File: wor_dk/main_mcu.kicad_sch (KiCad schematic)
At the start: 36 parts, among them J201 Prog_DUT, SW201 SW_Push, U201 nRF52840, U202 TMUX1112PWR, U203 TMUX1112PWR, Y201 32.768kHz, Y202 32MHz

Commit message: wor_dk: add footprints & part info for all capacitors
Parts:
- C201, C202, C203, C206, C209, C217: MPN (none) -> GRM033R61E104KE14D
- C204, C218, C219: MPN (none) -> CL10A105KB8NNNC
- C205: MPN (none) -> CL10A475KO8NNNC
- C207: footprint Resistor_SMD:R_0603_1608Metric -> Capacitor_SMD:C_0603_1608Metric; MPN (none) -> CL10A105KB8NNNC
- C208: footprint Resistor_SMD:R_0201_0603Metric -> Capacitor_SMD:C_0201_0603Metric; MPN (none) -> GRT033R60J473KE01D
- C211: MPN (none) -> GRM0335C1H101JA01D
- C212: MPN (none) -> GRM033R71E821KA01D
- C213, C214: MPN (none) -> GCM1555C1H220FA16D
- C215, C216: MPN (none) -> GJM1555C1H130FB01D
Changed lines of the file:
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@@
 			)
 		)
-		(property "Datasheet" "~"
+		(property "Datasheet" "https://wmsc.lcsc.com/wmsc/upload/file/pdf/v2/lcsc/1811081532_Murata-Electronics-GRM033R61E104KE14D_C76939.pdf"
 			(at 31.75 167.64 0)
 			(effects
@@
 			)
 		)
+		(property "MPN" "GRM033R61E104KE14D"
+			(at 31.75 167.64 0)
+			(effects
+				(font
+					(size 1.27 1.27)
+				)
+				(hide yes)
+			)
+		)
 		(pin "1"
 		)
@@
 			)
 		)
-		(property "Datasheet" "~"
+		(property "Datasheet" "https://wmsc.lcsc.com/wmsc/upload/file/pdf/v2/lcsc/2304140030_Samsung-Electro-Mechanics-CL10A105KB8NNNC_C15849.pdf"
 			(at 238.76 95.25 0)
 			(effects
@@
 			)
 		)
+		(property "MPN" "CL10A105KB8NNNC"
+			(at 238.76 95.25 0)
+			(effects
+				(font
+					(size 1.27 1.27)
+				)
+				(hide yes)
+			)
+		)
 		(pin "1"
 		)
@@
 			)
 		)
-		(property "Datasheet" "~"
+		(property "Datasheet" "https://wmsc.lcsc.com/wmsc/upload/file/pdf/v2/lcsc/1811081532_Murata-Electronics-GRM033R61E104KE14D_C76939.pdf"
 			(at 162.56 24.13 0)
 			(effects
@@
 			)
 		)
+		(property "MPN" "GRM033R61E104KE14D"
+			(at 162.56 24.13 0)
+			(effects
+				(font
+					(size 1.27 1.27)
+				)
+				(hide yes)
+			)
+		)
 		(pin "1"
 		)
@@
 			)
 		)
-		(property "Datasheet" "~"
+		(property "Datasheet" "https://wmsc.lcsc.com/wmsc/upload/file/pdf/v2/lcsc/1811081545_Murata-Electronics-GRM033R71E821KA01D_C185597.pdf"
 			(at 49.53 44.45 0)
 			(effects
@@
 			)
 		)
+		(property "MPN" "GRM033R71E821KA01D"
+			(at 49.53 44.45 0)
+			(effects
+				(font
+					(size 1.27 1.27)
+				)
+				(hide yes)
+			)
+		)
 		(pin "1"
 		)
@@
 			)
 		)
-		(property "Datasheet" "~"
+		(property "Datasheet" "https://wmsc.lcsc.com/wmsc/upload/file/pdf/v2/lcsc/1811081532_Murata-Electronics-GRM033R61E104KE14D_C76939.pdf"
 			(at 113.03 24.13 0)
 			(effects
@@
 			)
 		)
+		(property "MPN" "GRM033R61E104KE14D"
+			(at 113.03 24.13 0)
+			(effects
+				(font
+					(size 1.27 1.27)
+				)
+				(hide yes)
+			)
+		)
 		(pin "1"
 		)
@@
 			)
 		)
+		(property "MPN" "GCM1555C1H220FA16D"
+			(at 156.21 60.96 0)
+			(effects
+				(font
+					(size 1.27 1.27)
+				)
+				(hide yes)
+			)
+		)
 		(pin "1"
 		)
@@
 			)
 		)
-		(property "Datasheet" "~"
+		(property "Datasheet" "https://wmsc.lcsc.com/wmsc/upload/file/pdf/v2/lcsc/1811081532_Murata-Electronics-GRM033R61E104KE14D_C76939.pdf"
 			(at 15.24 44.45 0)
 			(effects
@@
 			)
 		)
+		(property "MPN" "GRM033R61E104KE14D"
+			(at 15.24 44.45 0)
+			(effects
+				(font
+					(size 1.27 1.27)
+				)
+				(hide yes)
+			)
+		)
 		(pin "1"
 		)
@@
 			)
 		)
+		(property "MPN" "GJM1555C1H130FB01D"
+			(at 27.94 123.19 0)
+			(effects
+				(font
+					(size 1.27 1.27)
+				)
+				(hide yes)
+			)
+		)
 		(pin "1"
 		)
@@
 			)
 		)
+		(property "MPN" "GCM1555C1H220FA16D"
+			(at 156.21 50.8 0)
+			(effects
+				(font
+					(size 1.27 1.27)
+				)
+				(hide yes)
+			)
+		)
 		(pin "1"
 		)
@@
 			)
 		)
-		(property "Datasheet" "~"
+		(property "Datasheet" "https://wmsc.lcsc.com/wmsc/upload/file/pdf/v2/lcsc/2304140030_Samsung-Electro-Mechanics-CL10A105KB8NNNC_C15849.pdf"
 			(at 138.43 24.13 0)
 			(effects
@@
 			)
 		)
+		(property "MPN" "CL10A105KB8NNNC"
+			(at 138.43 24.13 0)
+			(effects
+				(font
+					(size 1.27 1.27)
+				)
+				(hide yes)
+			)
+		)
 		(pin "1"
 		)
@@
 			)
 		)
-		(property "Datasheet" "~"
+		(property "Datasheet" "https://wmsc.lcsc.com/wmsc/upload/file/pdf/v2/lcsc/1811081532_Murata-Electronics-GRM033R61E104KE14D_C76939.pdf"
 			(at 101.6 24.13 0)
 			(effects
@@
 			)
 		)
+		(property "MPN" "GRM033R61E104KE14D"
+			(at 101.6 24.13 0)
+			(effects
+				(font
+					(size 1.27 1.27)
+				)
+				(hide yes)
+			)
+		)
 		(pin "1"
 		)
@@
 			)
 		)
-		(property "Datasheet" "~"
+		(property "Datasheet" "https://wmsc.lcsc.com/wmsc/upload/file/pdf/v2/lcsc/1811081532_Murata-Electronics-GRM033R61E104KE14D_C76939.pdf"
 			(at 124.46 24.13 0)
 			(effects
@@
 			)
 		)
+		(property "MPN" "GRM033R61E104KE14D"
+			(at 124.46 24.13 0)
+			(effects
+				(font
+					(size 1.27 1.27)
+				)
+				(hide yes)
+			)
+		)
 		(pin "1"
 		)
@@
 			)
 		)
+		(property "MPN" "GJM1555C1H130FB01D"
+			(at 27.94 113.03 0)
+			(effects
+				(font
+					(size 1.27 1.27)
+				)
+				(hide yes)
+			)
+		)
 		(pin "1"
 		)
@@
 			)
 		)
-		(property "Footprint" "Resistor_SMD:R_0201_0603Metric"
+		(property "Footprint" "Capacitor_SMD:C_0201_0603Metric"
 			(at 216.8652 40.64 0)
 			(effects
@@
 			)
 		)
-		(property "Datasheet" "~"
+		(property "Datasheet" "https://wmsc.lcsc.com/wmsc/upload/file/pdf/v2/lcsc/1811141821_Murata-Electronics-GRT033R60J473KE01D_C126621.pdf"
 			(at 215.9 36.83 0)
 			(effects
@@
 			)
 		)
+		(property "MPN" "GRT033R60J473KE01D"
+			(at 215.9 36.83 0)
+			(effects
+				(font
+					(size 1.27 1.27)
+				)
+				(hide yes)
+			)
+		)
 		(pin "1"
 		)
@@
 			)
 		)
-		(property "Datasheet" "~"
+		(property "Datasheet" "https://wmsc.lcsc.com/wmsc/upload/file/pdf/v2/lcsc/2304140030_Samsung-Electro-Mechanics-CL10A105KB8NNNC_C15849.pdf"
 			(at 226.06 151.13 0)
 			(effects
@@
 			)
 		)
+		(property "MPN" "CL10A105KB8NNNC"
+			(at 226.06 151.13 0)
+			(effects
+				(font
+					(size 1.27 1.27)
+				)
+				(hide yes)
+			)
+		)
 		(pin "1"
 		)
@@
 			)
 		)
-		(property "Footprint" "Resistor_SMD:R_0603_1608Metric"
+		(property "Footprint" "Capacitor_SMD:C_0603_1608Metric"
 			(at 206.7052 40.64 0)
 			(effects
@@
 			)
 		)
-		(property "Datasheet" "~"
+		(property "Datasheet" "https://wmsc.lcsc.com/wmsc/upload/file/pdf/v2/lcsc/2304140030_Samsung-Electro-Mechanics-CL10A105KB8NNNC_C15849.pdf"
 			(at 205.74 36.83 0)
 			(effects
@@
 			)
 		)
+		(property "MPN" "CL10A105KB8NNNC"
+			(at 205.74 36.83 0)
+			(effects
+				(font
+					(size 1.27 1.27)
+				)
+				(hide yes)
+			)
+		)
 		(pin "1"
 		)
@@
 			)
 		)
-		(property "Datasheet" "~"
+		(property "Datasheet" "https://wmsc.lcsc.com/wmsc/upload/file/pdf/v2/lcsc/2304140030_Samsung-Electro-Mechanics-CL10A475KO8NNNC_C19666.pdf"
 			(at 149.86 24.13 0)
 			(effects
@@
 			)
 		)
+		(property "MPN" "CL10A475KO8NNNC"
+			(at 149.86 24.13 0)
+			(effects
+				(font
+					(size 1.27 1.27)
+				)
+				(hide yes)
+			)
+		)
 		(pin "1"
 		)
@@
 			)
 		)
-		(property "Datasheet" "~"
+		(property "Datasheet" ""
 			(at 25.4 44.45 0)
 			(effects
@@
 			)
 		)
-		(property "Datasheet" "~"
+		(property "Datasheet" "https://wmsc.lcsc.com/wmsc/upload/file/pdf/v2/lcsc/1811081531_Murata-Electronics-GRM0335C1H101JA01D_C76922.pdf"
 			(at 35.56 44.45 0)
 			(effects
@@
 			(at 35.56 44.45 0)
 			(effects
+				(font
+					(size 1.27 1.27)
+				)
+				(hide yes)
+			)
+		)
+		(property "MPN" "GRM0335C1H101JA01D"
+			(at 35.56 44.45 0)
+			(effects

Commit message: wor_dk: exclude test points from BOM
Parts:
- TP201, TP202, TP203, TP204, TP205, TP206, TP207: now left out of the parts list
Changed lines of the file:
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@@
 		(unit 1)
 		(exclude_from_sim no)
-		(in_bom yes)
+		(in_bom no)
 		(on_board yes)
 		(dnp no)
@@
 			)
 		)
-		(property "Datasheet" "~"
+		(property "Datasheet" ""
 			(at 274.32 34.29 0)
 			(effects
@@
 		(unit 1)
 		(exclude_from_sim no)
-		(in_bom yes)
+		(in_bom no)
 		(on_board yes)
 		(dnp no)
@@
 			)
 		)
-		(property "Datasheet" "~"
+		(property "Datasheet" ""
 			(at 274.32 40.64 0)
 			(effects
@@
 		(unit 1)
 		(exclude_from_sim no)
-		(in_bom yes)
+		(in_bom no)
 		(on_board yes)
 		(dnp no)
@@
 			)
 		)
-		(property "Datasheet" "~"
+		(property "Datasheet" ""
 			(at 246.38 27.94 0)
 			(effects
@@
 		(unit 1)
 		(exclude_from_sim no)
-		(in_bom yes)
+		(in_bom no)
 		(on_board yes)
 		(dnp no)
@@
 			)
 		)
-		(property "Datasheet" "~"
+		(property "Datasheet" ""
 			(at 246.38 40.64 0)
 			(effects
@@
 		(unit 1)
 		(exclude_from_sim no)
-		(in_bom yes)
+		(in_bom no)
 		(on_board yes)
 		(dnp no)
@@
 			)
 		)
-		(property "Datasheet" "~"
+		(property "Datasheet" ""
 			(at 246.38 34.29 0)
 			(effects
@@
 		(unit 1)
 		(exclude_from_sim no)
-		(in_bom yes)
+		(in_bom no)
 		(on_board yes)
 		(dnp no)
@@
 			)
 		)
-		(property "Datasheet" "~"
+		(property "Datasheet" ""
 			(at 274.32 27.94 0)
 			(effects
@@
 		(unit 1)
 		(exclude_from_sim no)
-		(in_bom yes)
+		(in_bom no)
 		(on_board yes)
 		(dnp no)
@@
 			)
 		)
-		(property "Datasheet" "~"
+		(property "Datasheet" ""
 			(at 246.38 46.99 0)
 			(effects

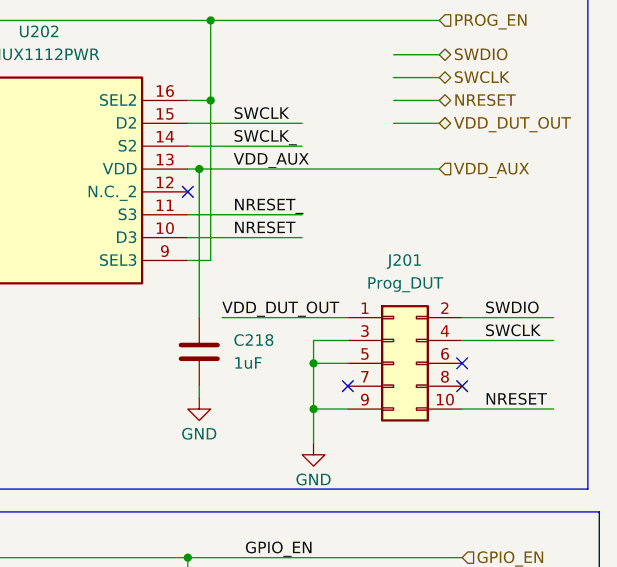
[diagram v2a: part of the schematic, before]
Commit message: wor_dk: add all footprints & part info for connectors
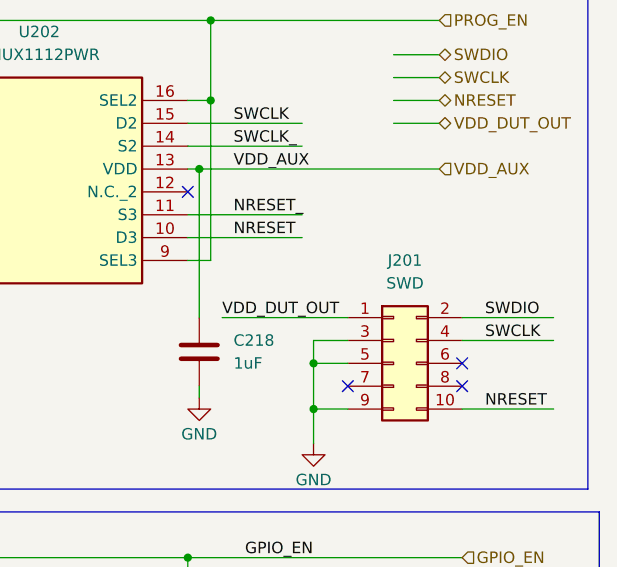
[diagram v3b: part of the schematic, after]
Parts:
- J201: value Prog_DUT -> SWD; Comment (none) -> Connector for debugging / flashing DUT using external progr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; LCSC (none) -> C598540; MPN (none) -> 20021121-00010T4LF; Manufacturer (none) -> Amphenol ICC
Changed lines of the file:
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@@
 			)
 		)
-		(property "Value" "Prog_DUT"
+		(property "Value" "SWD"
 			(at 261.62 87.63 0)
 			(effects
@@
 			)
 		)
-		(property "Datasheet" "~"
+		(property "Datasheet" "https://wmsc.lcsc.com/wmsc/upload/file/pdf/v2/lcsc/2204251545_Amphenol-ICC-20021121-00010T4LF_C598540.pdf"
 			(at 260.35 96.52 0)
 			(effects
@@
 			(at 260.35 96.52 0)
 			(effects
+				(font
+					(size 1.27 1.27)
+				)
+				(hide yes)
+			)
+		)
+		(property "Comment" "Connector for debugging / flashing DUT using external programmer"
+			(at 260.35 96.52 0)
+			(effects
+				(font
+					(size 1.27 1.27)
+				)
+				(hide yes)
+			)
+		)
+		(property "LCSC" "C598540"
+			(at 260.35 96.52 0)
+			(effects
+				(font
+					(size 1.27 1.27)
+				)
+				(hide yes)
+			)
+		)
+		(property "MPN" "20021121-00010T4LF"
+			(at 260.35 96.52 0)
+			(effects
+				(font
+					(size 1.27 1.27)
+				)
+				(hide yes)
+			)
+		)
+		(property "Manufacturer" "Amphenol ICC"
+			(at 260.35 96.52 0)
+			(effects

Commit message: wor_dk: assign footprint for test points
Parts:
- TP201, TP202, TP203, TP204, TP205, TP206, TP207: footprint (none) -> TestPoint:TestPoint_Pad_D2.0mm
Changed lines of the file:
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@@
 			)
 		)
-		(property "Footprint" ""
+		(property "Footprint" "TestPoint:TestPoint_Pad_D2.0mm"
 			(at 274.32 34.29 0)
 			(effects
@@
 			)
 		)
-		(property "Footprint" ""
+		(property "Footprint" "TestPoint:TestPoint_Pad_D2.0mm"
 			(at 274.32 40.64 0)
 			(effects
@@
 			)
 		)
-		(property "Footprint" ""
+		(property "Footprint" "TestPoint:TestPoint_Pad_D2.0mm"
 			(at 246.38 27.94 0)
 			(effects
@@
 			)
 		)
-		(property "Footprint" ""
+		(property "Footprint" "TestPoint:TestPoint_Pad_D2.0mm"
 			(at 246.38 40.64 0)
 			(effects
@@
 			)
 		)
-		(property "Footprint" ""
+		(property "Footprint" "TestPoint:TestPoint_Pad_D2.0mm"
 			(at 246.38 34.29 0)
 			(effects
@@
 			)
 		)
-		(property "Footprint" ""
+		(property "Footprint" "TestPoint:TestPoint_Pad_D2.0mm"
 			(at 274.32 27.94 0)
 			(effects
@@
 			)
 		)
-		(property "Footprint" ""
+		(property "Footprint" "TestPoint:TestPoint_Pad_D2.0mm"
 			(at 246.38 46.99 0)
 			(effects

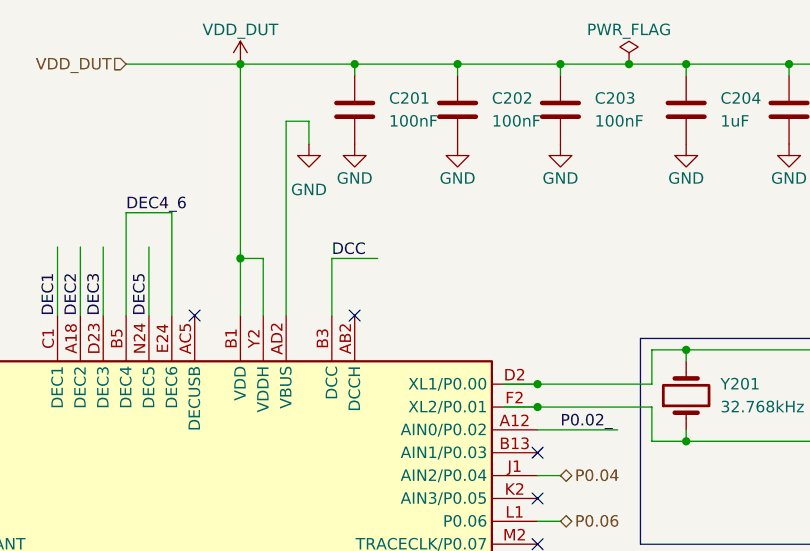
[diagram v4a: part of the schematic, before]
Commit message: wor_dk: schematic: MCU: add test point for DCCH
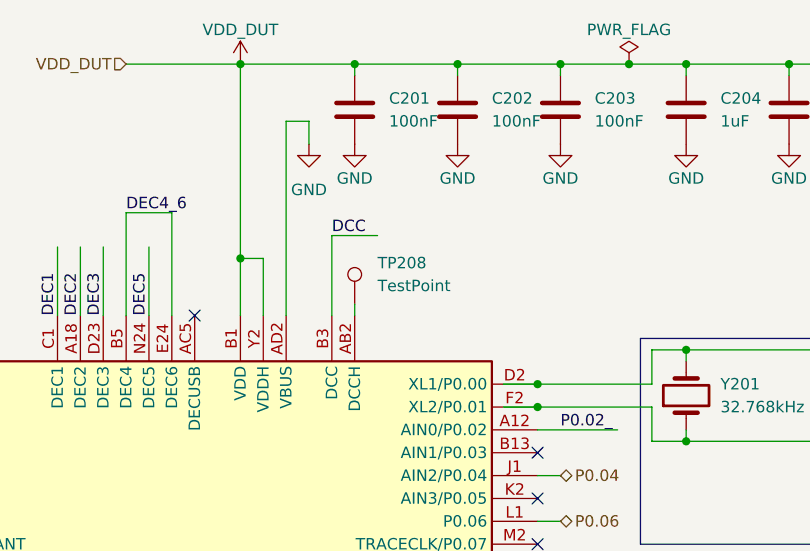
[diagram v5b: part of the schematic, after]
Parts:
- added TP208: TestPoint, TestPoint:TestPoint_Pad_D2.0mm, symbol Connector:TestPoint
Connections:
- net at U201.AB2 (DCCH): now also TP208.1
- no-connect marks 42 -> 41
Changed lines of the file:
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@@
 	)
 	(no_connect
-		(at 101.6 46.99)
-	)
-	(no_connect
 		(at 121.92 72.39)
 	)
@@
 	(wire
 		(pts
-			(xy 99.06 40.64) (xy 104.14 40.64)
+			(xy 99.06 38.1) (xy 104.14 38.1)
 		)
 		(stroke
@@
 	(wire
 		(pts
+			(xy 101.6 45.72) (xy 101.6 46.99)
+		)
+		(stroke
+			(width 0)
+			(type default)
+		)
+	)
+	(wire
+		(pts
 			(xy 134.62 54.61) (xy 134.62 50.8)
 		)
@@
 	(wire
 		(pts
-			(xy 99.06 46.99) (xy 99.06 40.64)
+			(xy 99.06 46.99) (xy 99.06 38.1)
 		)
 		(stroke
@@
 	)
 	(label "DCC"
-		(at 99.06 40.64 0)
+		(at 99.06 38.1 0)
 		(fields_autoplaced yes)
 		(effects
@@
 					(unit 1)
 				)
+			)
+		)
+	)
+	(symbol
+		(lib_id "Connector:TestPoint")
+		(at 101.6 45.72 0)
+		(unit 1)
+		(exclude_from_sim no)
+		(in_bom no)
+		(on_board yes)
+		(dnp no)
+		(fields_autoplaced yes)
+		(property "Reference" "TP208"
+			(at 104.14 41.1479 0)
+			(effects
+				(font
+					(size 1.27 1.27)
+				)
+				(justify left)
+			)
+		)
+		(property "Value" "TestPoint"
+			(at 104.14 43.6879 0)
+			(effects
+				(font
+					(size 1.27 1.27)
+				)
+				(justify left)
+			)
+		)
+		(property "Footprint" "TestPoint:TestPoint_Pad_D2.0mm"
+			(at 106.68 45.72 0)
+			(effects
+				(font
+					(size 1.27 1.27)
+				)
+				(hide yes)
+			)
+		)
+		(property "Datasheet" ""
+			(at 106.68 45.72 0)
+			(effects
+				(font
+					(size 1.27 1.27)
+				)
+				(hide yes)
+			)
+		)
+		(property "Description" "test point"
+			(at 101.6 45.72 0)
+			(effects
+				(font
+					(size 1.27 1.27)
+				)
+				(hide yes)
+			)
+		)
+		(pin "1"
+		)
+		(instances
+			(project "wor_dk"
+				(path "/8d3147eb-060b-4f65-bf42-ed06a58b21ba/9b741a5c-1fa6-4ec7-876c-f0b1f25b18e4"
+					(reference "TP208")
+					(unit 1)
+				)

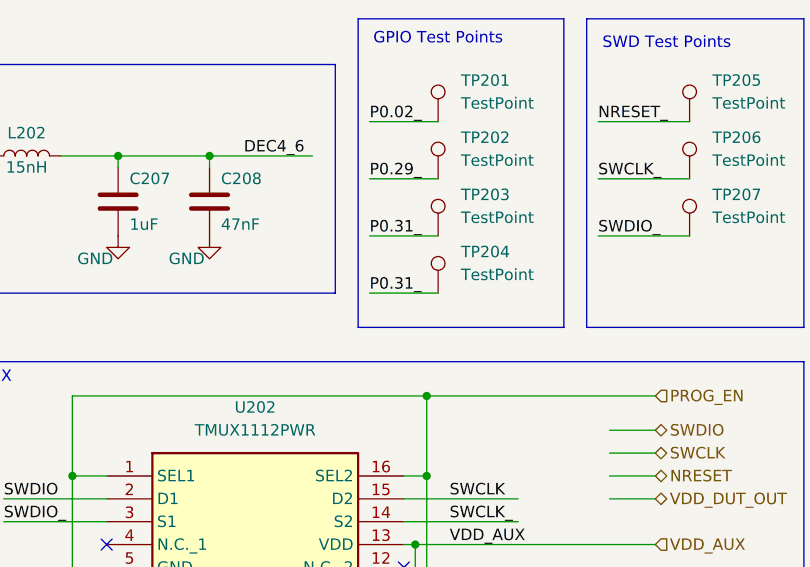
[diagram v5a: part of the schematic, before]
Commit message: wor_dk: schematic: fix test points
Removed accidental second test point for P0.31_, added one for P1.02_.
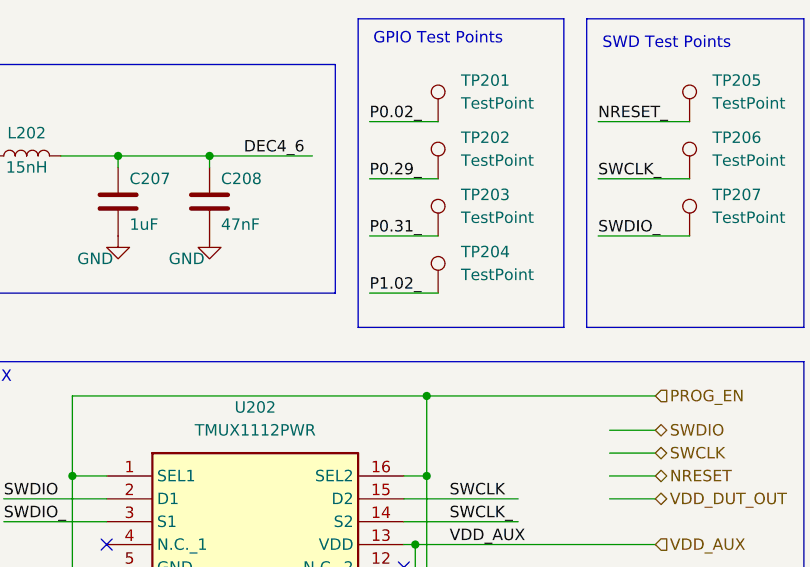
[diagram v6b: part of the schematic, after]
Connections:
- net P0.31_: no longer TP204.1
- net P1.02_: now also TP204.1
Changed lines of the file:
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@@
-		)
-	)
-	(label "P0.31_"
-		(at 233.68 46.99 0)
-		(fields_autoplaced yes)
-		(effects
-			(font
-				(size 1.27 1.27)
-			)
-			(justify left bottom)
 		)
 	)
@@
 		(fields_autoplaced yes)
 		(effects
+			(font
+				(size 1.27 1.27)
+			)
+			(justify left bottom)
+		)
+	)
+	(label "P1.02_"
+		(at 233.68 46.99 0)
+		(fields_autoplaced yes)
+		(effects
